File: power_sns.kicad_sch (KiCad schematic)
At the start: 3 parts, among them U18 PINA745AIRELR

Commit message: Schematic updates
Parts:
- U18: Mfr (none) -> Texas Instruments; Mfr P/N (none) -> INA745BIRELR; Supplier_1 (none) -> JLCPCB; Supplier_1 P/N (none) -> C35213810
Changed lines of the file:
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@@
 			)
 		)
-		(property "Mfr" ""
+		(property "Mfr" "Texas Instruments"
 			(at 170.18 76.2 0)
 			(effects
@@
 			)
 		)
-		(property "Mfr P/N" ""
+		(property "Mfr P/N" "INA745BIRELR"
 			(at 170.18 76.2 0)
 			(effects
@@
 			)
 		)
-		(property "Supplier_1" ""
+		(property "Supplier_1" "JLCPCB"
 			(at 170.18 76.2 0)
 			(effects
@@
 			)
 		)
-		(property "Supplier_1 P/N" ""
+		(property "Supplier_1 P/N" "C35213810"
 			(at 170.18 76.2 0)
 			(effects

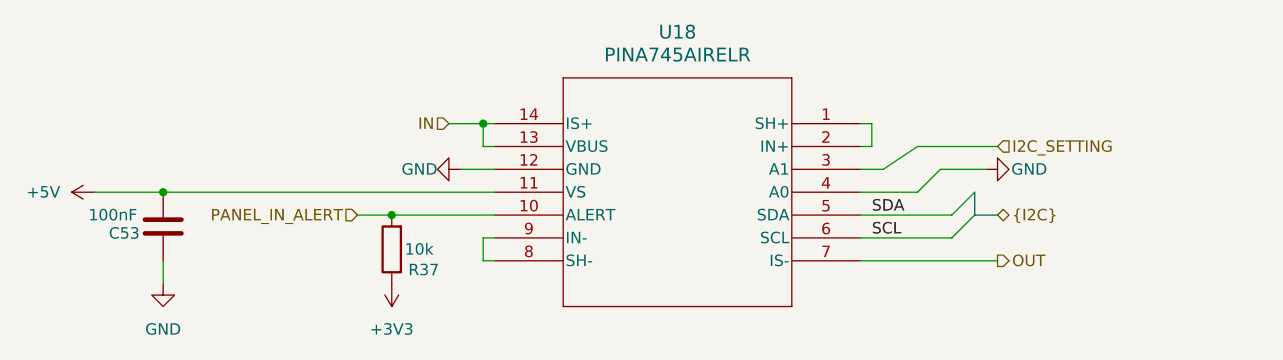
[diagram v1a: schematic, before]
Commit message: i2c 0 and 1 bus routed + mosfet logic change
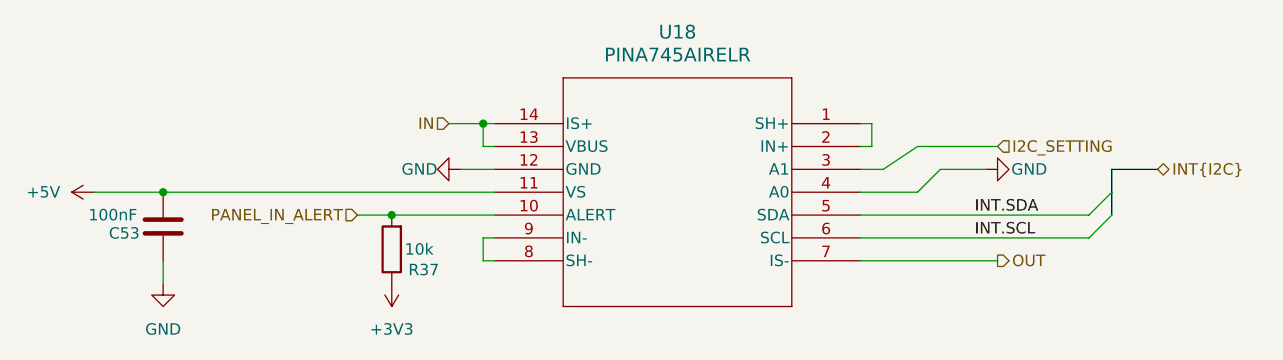
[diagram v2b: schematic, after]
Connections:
- net SCL renamed INT.SCL
- net SDA renamed INT.SDA
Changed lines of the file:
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@@
 	)
 	(bus_entry
-		(at 180.34 88.9)
-		(size 2.54 -2.54)
+		(at 198.12 83.82)
+		(size -2.54 2.54)
 		(stroke
 			(width 0)
@@
 	)
 	(bus_entry
-		(at 180.34 86.36)
-		(size 2.54 -2.54)
+		(at 198.12 86.36)
+		(size -2.54 2.54)
 		(stroke
 			(width 0)
@@
 		)
 	)
+	(bus
+		(pts
+			(xy 198.12 83.82) (xy 198.12 81.28)
+		)
+		(stroke
+			(width 0)
+			(type default)
+		)
+	)
 	(wire
 		(pts
@@
 		)
 	)
+	(bus
+		(pts
+			(xy 198.12 81.28) (xy 203.2 81.28)
+		)
+		(stroke
+			(width 0)
+			(type default)
+		)
+	)
 	(wire
 		(pts
@@
 	(bus
 		(pts
-			(xy 182.88 86.36) (xy 185.42 86.36)
+			(xy 198.12 86.36) (xy 198.12 83.82)
 		)
 		(stroke
@@
 		)
 	)
-	(bus
-		(pts
-			(xy 182.88 83.82) (xy 182.88 86.36)
-		)
-		(stroke
-			(width 0)
-			(type default)
-		)
-	)
 	(wire
 		(pts
-			(xy 170.18 88.9) (xy 180.34 88.9)
+			(xy 170.18 88.9) (xy 195.58 88.9)
 		)
 		(stroke
@@
 	(wire
 		(pts
-			(xy 170.18 86.36) (xy 180.34 86.36)
+			(xy 170.18 86.36) (xy 195.58 86.36)
 		)
 		(stroke
@@
 		)
 	)
-	(label "SDA"
-		(at 171.45 86.36 0)
+	(label "INT.SCL"
+		(at 182.88 88.9 0)
 		(effects
 			(font
@@
 		)
 	)
-	(label "SCL"
-		(at 171.45 88.9 0)
+	(label "INT.SDA"
+		(at 182.88 86.36 0)
 		(effects
 			(font
@@
 		)
 	)
-	(hierarchical_label "{I2C}"
-		(shape bidirectional)
-		(at 185.42 86.36 0)
-		(effects
-			(font
-				(size 1.27 1.27)
-			)
-			(justify left)
-		)
-	)
 	(hierarchical_label "IN"
 		(shape input)
@@
 		(effects
 			(font
+				(size 1.27 1.27)
+			)
+			(justify left)
+		)
+	)
+	(hierarchical_label "INT{I2C}"
+		(shape bidirectional)
+		(at 203.2 81.28 0)
+		(effects
+			(font
